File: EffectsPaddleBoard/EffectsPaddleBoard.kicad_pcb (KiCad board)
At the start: 4 copper layers, 89.6 x 66.6 mm, 90 parts, among them J1 Conn_01x03_Pin, J2 Conn_01x06_Pin, J3 Barrel_Jack, J4 Conn_01x04_Pin, J5 AudioJack2, J6 AudioJack2, SW1 SW_SPDT, SW2 SW_Push, SW4 SW_Push, U1 STM32F405RGTx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

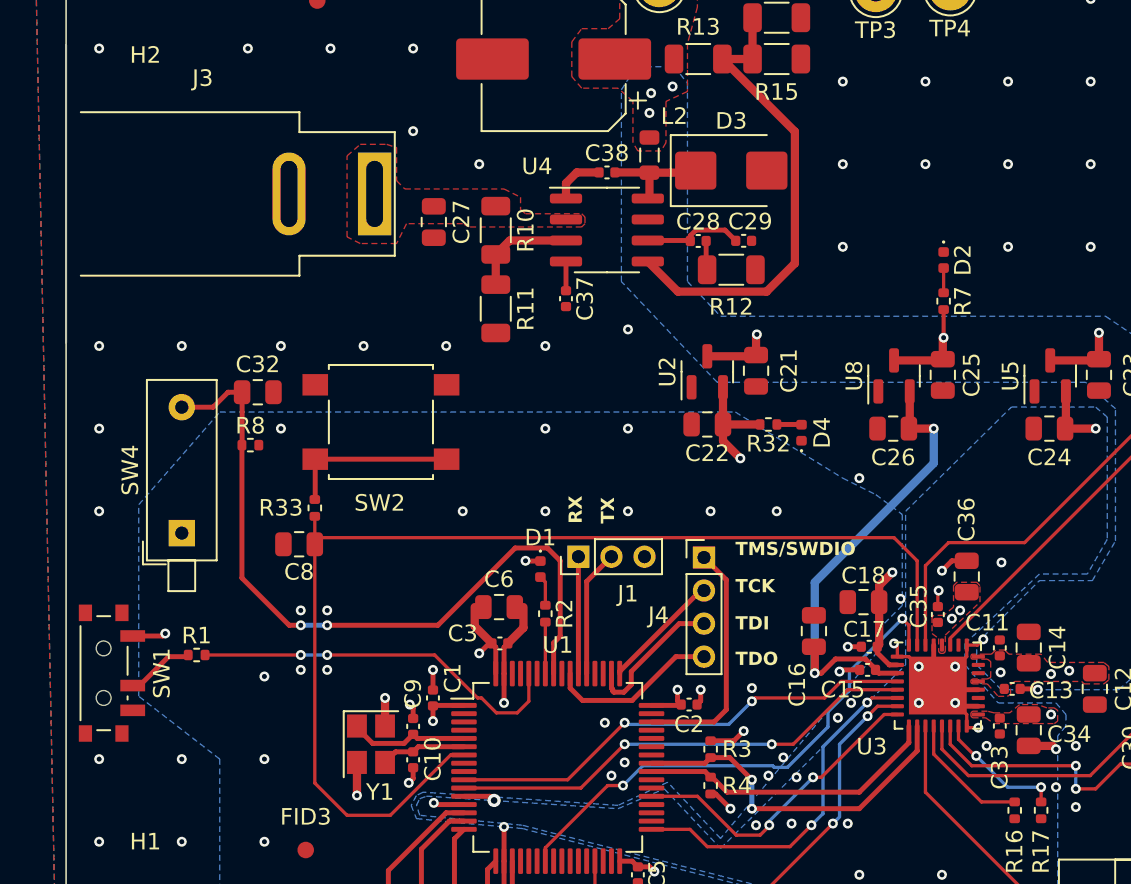
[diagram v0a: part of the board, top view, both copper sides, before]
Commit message: Added further testpoints
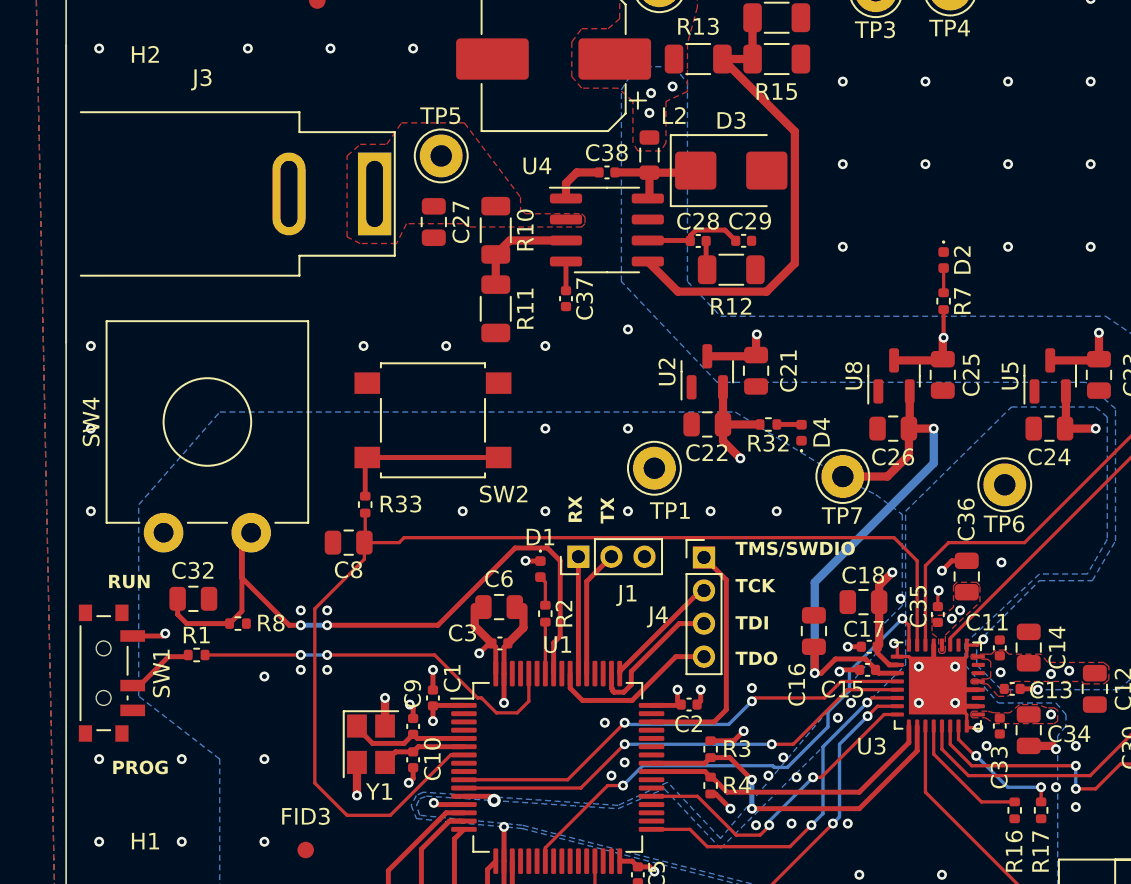
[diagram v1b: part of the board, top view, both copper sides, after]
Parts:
- added TP1: TestPoint, Connector_Pin:Pin_D1.3mm_L11.0mm, F.Cu at (156.6, 82.4)
- added TP5: TestPoint, Connector_Pin:Pin_D1.3mm_L11.0mm, F.Cu at (143.7, 63.5)
- added TP6: TestPoint, Connector_Pin:Pin_D1.3mm_L11.0mm, F.Cu at (177.8, 83.4)
- added TP7: TestPoint, Connector_Pin:Pin_D1.3mm_L11.0mm, F.Cu at (168.0, 82.9)
- SW4: footprint Button_Switch_THT:SW_DIP_SPSTx01_Piano_10.8x4.1mm_W7.62mm_P2.54mm -> Button_Switch_THT:SW_CW_GPTS203211B
- moved C32 13.1 mm to (128.7, 90.3)
- moved R8 10.8 mm to (131.4, 91.8)
- moved SW2 3.15 mm to (143.2, 79.5)
- moved R33 3.06 mm to (139.1, 84.6)
- moved C8 3.00 mm to (138.1, 86.9)
- moved SW4 1.10 mm to (126.9, 86.3)
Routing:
- net +1V8: track 29.1 -> 35.2 mm
- net On-Switch: track 45.0 -> 41.9 mm
- net Codec_Reset: track 69.8 -> 68.2 mm
- net GND: vias 137 -> 131
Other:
- board text added: "PROG"
- board text added: "RUN"

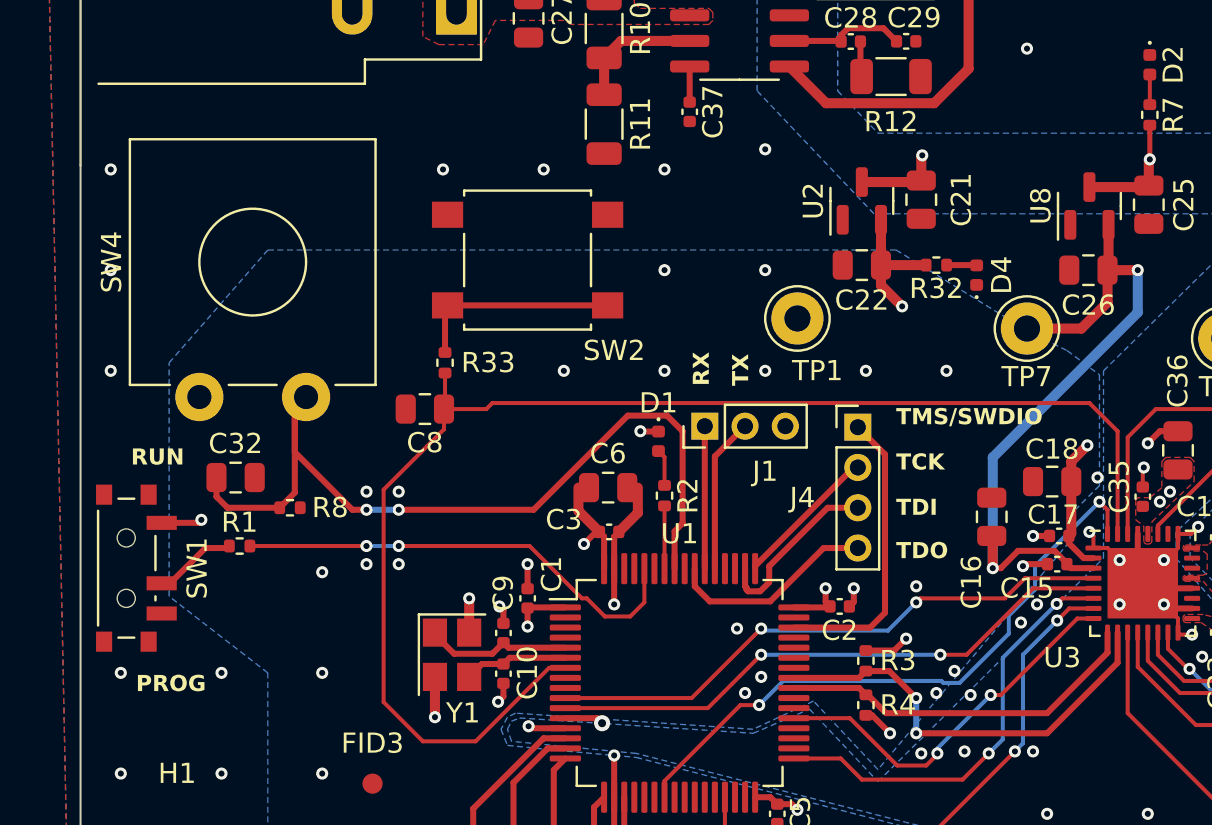
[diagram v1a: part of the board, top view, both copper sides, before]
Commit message: Added better switch footprint
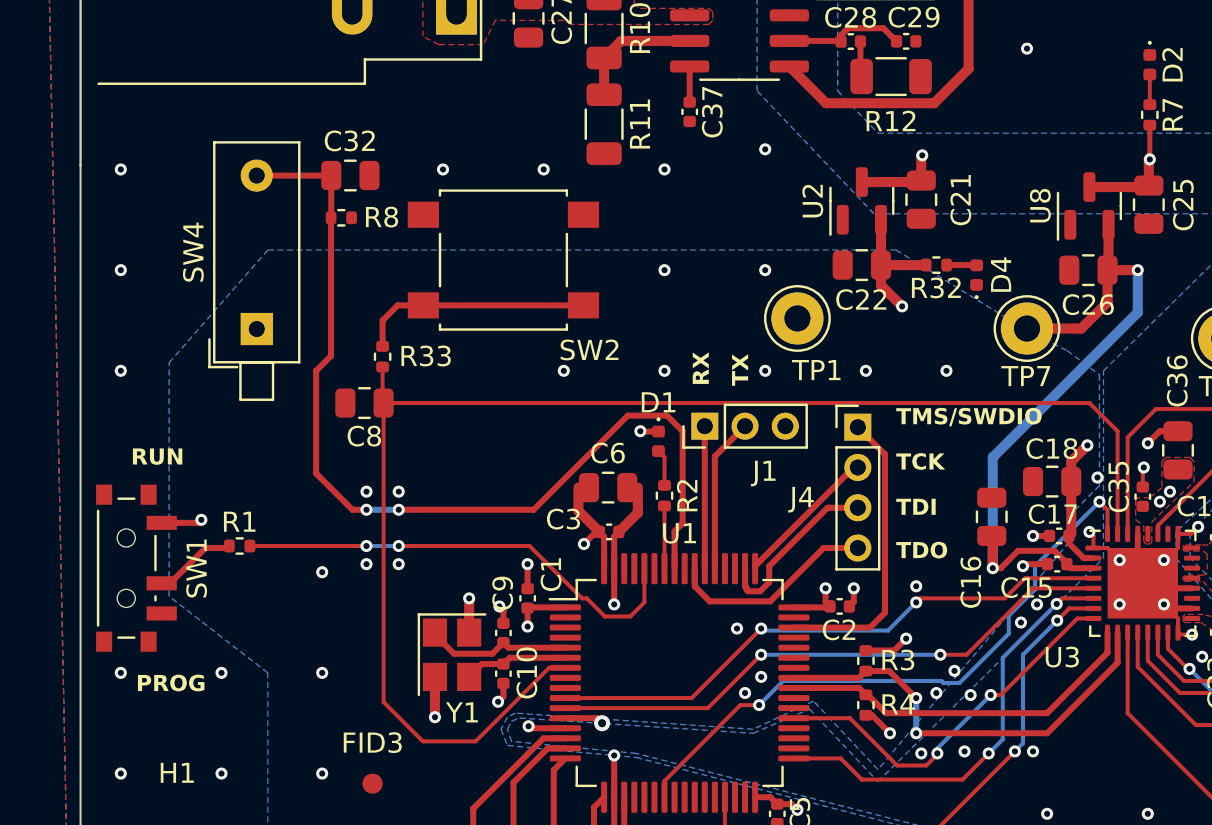
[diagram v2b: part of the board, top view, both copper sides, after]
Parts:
- SW4: footprint Button_Switch_THT:SW_CW_GPTS203211B -> Button_Switch_THT:SW_DIP_SPSTx01_Piano_10.8x4.1mm_W7.62mm_P2.54mm
- moved C32 16.0 mm to (134.4, 75.3)
- moved R8 14.6 mm to (133.9, 77.4)
- moved SW4 4.42 mm to (129.8, 82.9)
- moved R33 3.11 mm to (136.0, 84.3)
- moved C8 3.01 mm to (135.1, 86.6)
- moved SW2 1.20 mm to (142.0, 79.5)
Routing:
- net On-Switch: track 41.9 -> 47.0 mm
- net Codec_Reset: track 68.2 -> 70.1 mm
- net Net-(R33-Pad1): track 10.3 -> 11.6 mm

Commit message: exported symbols and footprints, updated PCB
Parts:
- removed C27: 10u, Capacitor_SMD:C_0805_2012Metric
- removed C28, C29: 220p, Capacitor_SMD:C_0402_1005Metric
- removed C37: 15n, Capacitor_SMD:C_0402_1005Metric
- removed C38: 100n, Capacitor_SMD:C_0402_1005Metric
- removed C39: 470u, Capacitor_SMD:CP_Elec_8x10.5
- removed D3: B230, Diode_SMD:D_SMB
- removed L2: 15u, Inductor_SMD:L_0805_2012Metric
- removed R11: 68.1k, Resistor_SMD:R_1206_3216Metric
- removed R12: 30.9k, Resistor_SMD:R_1206_3216Metric
- removed R13: 10k, Resistor_SMD:R_1206_3216Metric
- removed R14, R15: 3.9k, Resistor_SMD:R_1206_3216Metric
- removed U4: TPS54233, Package_SO:SOIC-8_3.9x4.9mm_P1.27mm
- added C40: 10u, Capacitor_SMD:C_0805_2012Metric, F.Cu at (143.2, 102.1)
- added C41: 22u, Capacitor_SMD:C_0805_2012Metric, F.Cu at (153.8, 68.1)
- added C42: 22u, Capacitor_SMD:C_0805_2012Metric, F.Cu at (155.9, 68.1)
- added C46: 100n, Capacitor_SMD:C_0402_1005Metric, F.Cu at (153.2, 63.6)
- added C47: 10u, Capacitor_SMD:C_0805_2012Metric, F.Cu at (149.0, 63.7)
- added C7: 100n, Capacitor_SMD:C_0402_1005Metric, F.Cu at (144.8, 102.2)
- added L1: 2.2u, Inductor_SMD:L_1210_3225Metric, F.Cu at (151.0, 68.1)
- added R19: 10k, Resistor_SMD:R_0402_1005Metric, F.Cu at (148.6, 67.0)
- added R9: 52.3k, Resistor_SMD:R_0402_1005Metric, F.Cu at (148.6, 69.1)
- added U6: AP62250Z6, Package_TO_SOT_SMD:SOT-563, F.Cu at (151.4, 64.0)
- J3: footprint Connector_BarrelJack:BarrelJack_SwitchcraftConxall_RAPC10U_Horizontal -> Library:BarrelJack_SwitchcraftConxall_RAPC10U_Horizontal
- R10: value 332k -> 220; footprint Resistor_SMD:R_1206_3216Metric -> Resistor_SMD:R_0402_1005Metric
- SW4: footprint Button_Switch_THT:SW_DIP_SPSTx01_Piano_10.8x4.1mm_W7.62mm_P2.54mm -> Button_Switch_THT:SW_CW_GPTS203211B
- moved R10 20.4 mm to (149.2, 88.3), turned to 90 degrees
- moved R6 19.7 mm to (178.4, 87.2), turned to -90 degrees
- moved TP2 19.6 mm to (153.9, 72.6)
- moved C31 19.1 mm to (180.7, 87.2), turned to 0 degrees
- moved C20 18.5 mm to (180.7, 89.4), turned to 0 degrees
- moved C32 18.5 mm to (147.4, 88.4), turned to -90 degrees
- moved D2 16.4 mm to (158.1, 66.3)
- moved R7 16.4 mm to (158.1, 68.8)
- moved R8 15.1 mm to (145.2, 87.4), turned to 180 degrees
- moved C19 11.6 mm to (180.1, 103.9)
- moved C8 9.56 mm to (144.4, 84.4), turned to 0 degrees
- moved R18 9.55 mm to (168.8, 111.5)
- moved RV1 9.55 mm to (174.1, 112.0)
- moved R23 9.53 mm to (177.6, 101.7), turned to 90 degrees
- moved R5 8.18 mm to (182.5, 102.8), turned to 90 degrees
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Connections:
- R10 pad 1: /Barreljack_in -> GND
- R10 pad 2: /en5v -> On-Switch
- R8 pad 2: GND -> Net-(R8-Pad2)
- SW4 pad 2: On-Switch -> Net-(R8-Pad2)
- U3 pad 23: unconnected-(U3-SPKM-Pad19) -> unconnected-(U3-SPKM-Pad23)
- U3 pad 26: unconnected-(U3-SPKP-Pad22) -> unconnected-(U3-SPKP-Pad26)
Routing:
- net +3.3V: track 35.8 -> 154.4 mm, vias 10 -> 9
- net +3.3VA: track 6.88 -> 86.5 mm, vias 6 -> 4
- net +5V: track 14.8 -> 65.0 mm, vias 9 -> 1
- net On-Switch: track 47.0 -> 13.0 mm, vias 2 -> 0
- net Net-(U3-HPR): track 40.0 -> 8.58 mm
- net /fb5v: track 28.9 -> 0.00 mm
- net /Codec/HPL: track 26.9 -> 6.46 mm
- net /Codec/AudioOutBoard: track 8.19 -> 24.8 mm
- net Net-(R8-Pad2): track 0.00 -> 16.5 mm, vias 0 -> 1
- net /Barreljack_in: track 0.00 -> 12.3 mm
- net Net-(C19-Pad2): track 7.60 -> 19.2 mm
- net Codec_Reset: track 70.1 -> 58.8 mm, vias 0 -> 2
- net /Codec/Analog_In_R: track 18.1 -> 7.12 mm, vias 2 -> 0
- net /v_fb: track 0.00 -> 10.1 mm, vias 0 -> 2
- net /Codec/Analog_In_L: track 17.9 -> 8.35 mm
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- removed copper zone on B.Cu, net +3.3V
- removed copper zone on B.Cu, net +3.3VA
- removed copper zone on B.Cu, net +5V
- removed copper zone on F.Cu, net /Barreljack_in
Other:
- outline, holes or cut-outs redrawn
- board text added: "TODO: make outline interger valued millimeters"

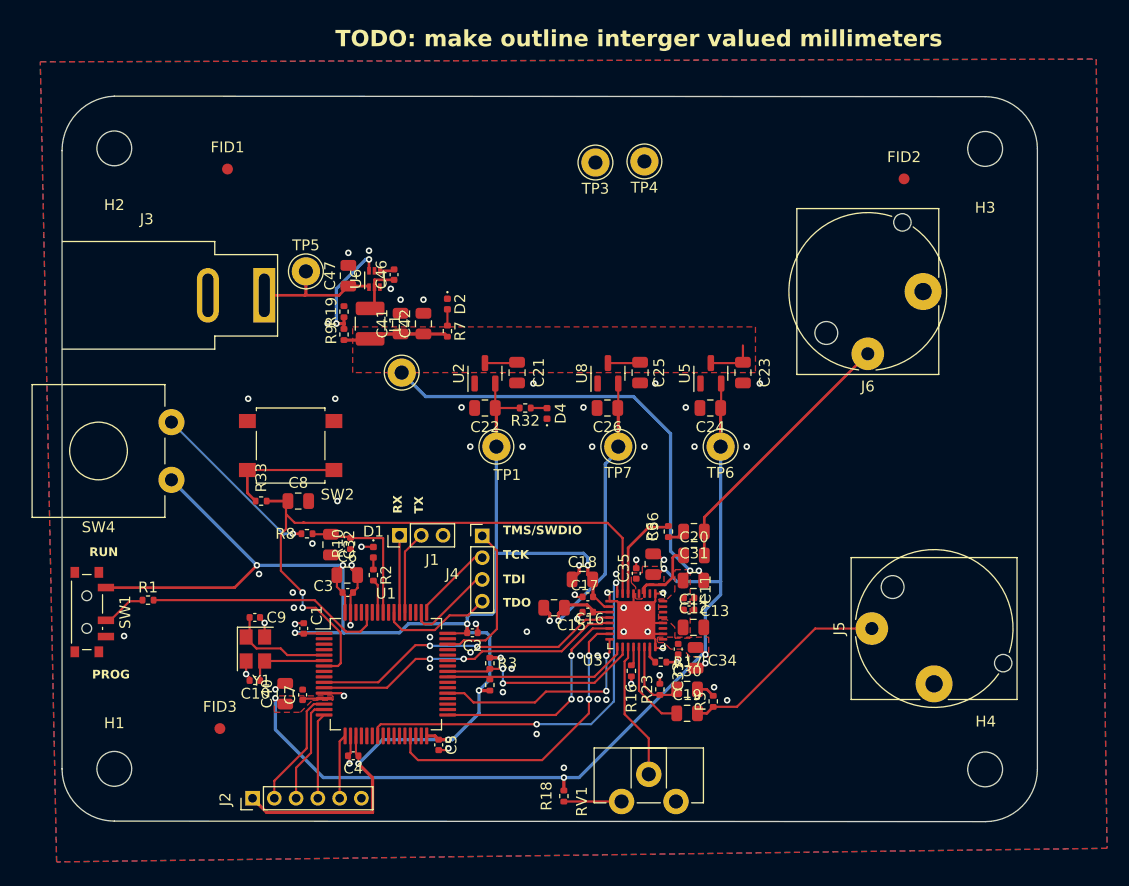
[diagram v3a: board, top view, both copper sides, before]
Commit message: Added new buck regulator, but footprint is missing
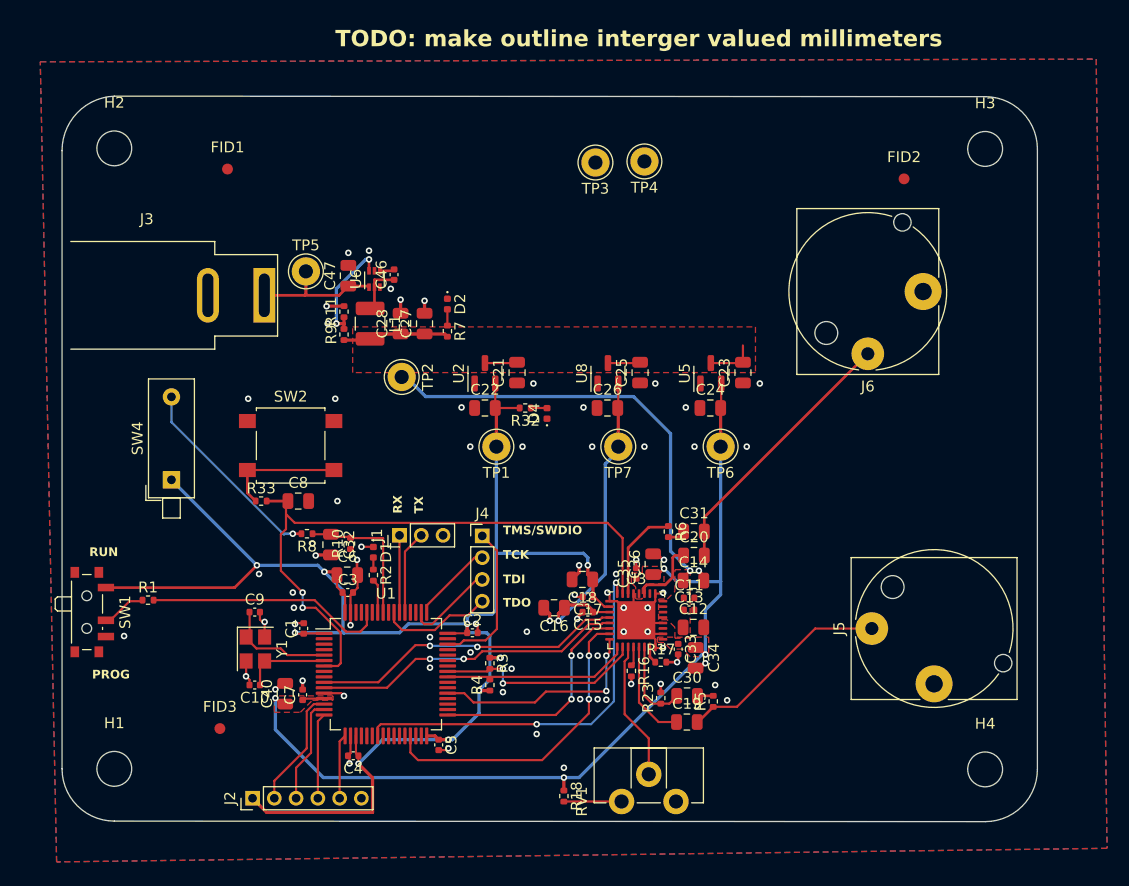
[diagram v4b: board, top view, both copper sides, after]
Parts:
- removed C41, C42: 22u, Capacitor_SMD:C_0805_2012Metric
- removed R19: 10k, Resistor_SMD:R_0402_1005Metric
- added C27: 22u, Capacitor_SMD:C_0805_2012Metric, F.Cu at (156.0, 68.1)
- added C28: 22u, Capacitor_SMD:C_0805_2012Metric, F.Cu at (153.8, 68.1)
- added R11: 10k, Resistor_SMD:R_0402_1005Metric, F.Cu at (148.6, 67.0)
- J3: footprint Library:BarrelJack_SwitchcraftConxall_RAPC10U_Horizontal -> EffectsPaddleBoard:BarrelJack_SwitchcraftConxall_RAPC10U_Horizontal
- SW4: footprint Button_Switch_THT:SW_CW_GPTS203211B -> EffectsPaddleBoard:SW_DIP_SPSTx01_Piano_10.8x4.1mm_W7.62mm_P2.54mm
- moved R23 0.80 mm to (177.7, 102.5)
- moved C19 0.80 mm to (180.1, 104.7)
- moved C30 0.60 mm to (180.1, 102.3)
- moved C9 0.49 mm to (140.4, 94.6)
- moved C10 0.41 mm to (140.4, 101.3)
- moved TP2 0.40 mm to (153.9, 73.0)
- turned SW4 to 90 degrees
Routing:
- net GND: track 47.2 -> 54.8 mm, vias 71 -> 74
- net Net-(R8-Pad2): track 16.5 -> 18.9 mm
- net /Codec/Analog_In_R: track 7.12 -> 8.08 mm
- net +3.3V: track 154.4 -> 153.5 mm
- net /Codec/Analog_In_L: track 8.35 -> 9.30 mm
